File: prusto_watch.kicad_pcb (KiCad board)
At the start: 4 copper layers, 45.7 x 40.6 mm, 79 parts, among them J1 USB_microB_2040002-1, J3 Conn_02x05_Odd_Even, J4 Vibration Motor, J6 Conn_01x05, Q1 RUM002N02T2L, Q2 RUM002N02T2L, Q3 RUM002N02T2L, SW1 SW_Push, SW2 SW_Push, U1 STM32F303RCT6-48, U2 TPS2113ADRBR, U3 TSP70933DBVR, U4 MCP73831T-2ACI, U5 AT42QT1070-MMHR, U6 TPS60241DGKR, U7 RT9818A-18GV, U8 WM1389CT-ND, U9 LSM6DSL, Y1 ECS.327, Y2 FA-238

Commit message: Basic positioning
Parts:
- removed C27: 100nF, Capacitors_SMD:C_0603
- removed J6: Conn_01x05, Pin_Headers:Pin_Header_Straight_1x05_Pitch1.00mm
- removed R17, R18, R19, R20, R21, R22, R23: 10K, Resistors_SMD:R_0603
- removed R24: 4.75K, Resistors_SMD:R_0603
- removed R25: 1K, Resistors_SMD:R_0603
- removed R26: 100K, Resistors_SMD:R_0603
- removed U9: LSM6DSL, Housings_LGA:Bosch_LGA-14_3x2.5mm_Pitch0.5mm
- added J2: Conn_02x05_Odd_Even, Pin_Headers:Pin_Header_Straight_2x05_Pitch1.00mm, F.Cu at (117.8, 51.5)
- added J5: Conn_01x08, Pin_Headers:Pin_Header_Straight_1x08_Pitch2.54mm, F.Cu at (134.6, 163.8)
- BT1: value Battery_Cell -> RJD3032HPPV30M
- C1, C10, C11, C12, C13, C14, C15, C16, C18, C19, C2, C26, C3, C4, C5, C6, C7, C8, C9, R10, R2, R9: moved to F.Cu
- C17, C21: value 100nF -> 1uF; footprint Capacitors_SMD:C_0603 -> Capacitors_SMD:C_0805; moved to F.Cu
- C20, C22, C23: value 1uF -> 100nF; footprint Capacitors_SMD:C_0805 -> Capacitors_SMD:C_0603; moved to F.Cu
- C24: value 10uF -> 1uF; moved to F.Cu
- C25: value 100nF -> 10uF; footprint Capacitors_SMD:C_0603 -> Capacitors_SMD:C_0805; moved to F.Cu
- D2: footprint open_watch:SMLP34RGB2W3 -> prusto_watch:SMLP34RGB2W3
- FP1: footprint open_watch:BM71BLES1FC2 -> prusto_watch:BM71BLES1FC2
- J1: footprint open_watch:USB_microB_2040002-1 -> prusto_watch:USB_microB_2040002-1
- J3: value Conn_02x05_Odd_Even -> Vibration Motor; footprint Pin_Headers:Pin_Header_Straight_2x05_Pitch1.00mm -> Pin_Headers:Pin_Header_Straight_1x02_Pitch1.00mm
- J4: value Vibration Motor -> Conn_01x06; footprint Pin_Headers:Pin_Header_Straight_1x02_Pitch1.00mm -> Pin_Headers:Pin_Header_Straight_1x06_Pitch2.54mm
- Q1, Q2, Q3: footprint open_watch:VMT3 -> prusto_watch:VMT3
- R1: value 10K -> 100K; moved to F.Cu
- R11: value DNP-0 -> 1K; moved to F.Cu
- R12: value 100K -> DNP-0; moved to F.Cu
- R14: value 10K -> 4.75K
- R15: value 10K -> 1K
- R3: value 402 -> 10K; moved to F.Cu
- R4: value 200K -> 100K; moved to F.Cu
- R5: value 470 -> 402; moved to F.Cu
- R6: value 1K -> 200K; moved to F.Cu
- R7: value 1K -> 470; moved to F.Cu
- R8: value 10K -> 1K; moved to F.Cu
- SW1, SW2: footprint open_watch:PTS820_J15M_SMTR_LFS -> prusto_watch:PTS820_J15M_SMTR_LFS
- U2: footprint open_watch:SON-8 -> prusto_watch:SON-8
- U5: value AT42QT1070-MMHR -> TPS60241DGKR; footprint open_watch:AT42QT1070-MMHR -> Housings_SSOP:MSOP-8_3x3mm_Pitch0.65mm
- U6: value TPS60241DGKR -> LSM6DSL; footprint Housings_SSOP:MSOP-8_3x3mm_Pitch0.65mm -> Housings_LGA:Bosch_LGA-14_3x2.5mm_Pitch0.5mm
- U8: footprint open_watch:Molex_FPC_5034801000 -> prusto_watch:Molex_FPC_5034801000
- Y1: footprint open_watch:ECX-31B -> prusto_watch:ECX-31B
- moved R2 178.5 mm to (242.3, 108.0)
- moved R1 176.6 mm to (232.1, 119.5), turned to 0 degrees
- moved C5 169.8 mm to (223.3, 111.3)
- moved D3 169.7 mm to (210.6, 121.3), turned to 0 degrees
- moved R13 169.4 mm to (215.6, 137.3), turned to 0 degrees
- moved R10 164.1 mm to (212.6, 38.1), turned to 0 degrees
- moved Q2 154.1 mm to (203.6, 111.3)
- moved U6 148.2 mm to (186.7, 155.5)
- moved C14 145.6 mm to (213.6, 43.2), turned to 0 degrees
- moved C23 141.0 mm to (193.6, 157.5)
- moved C22 140.7 mm to (189.8, 149.9), turned to 0 degrees
- moved BT1 140.7 mm to (190.6, 112.3), turned to 0 degrees
- moved R7 140.6 mm to (210.1, 48.3), turned to 0 degrees
- moved J3 140.5 mm to (207.0, 105.6), turned to 0 degrees
- moved Q3 140.0 mm to (184.2, 119.4), turned to 0 degrees
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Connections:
- C18 pad 1: +3V3 -> Net-(C18-Pad1)
- C18 pad 2: GND -> Net-(C18-Pad2)
- C20 pad 1: Net-(C20-Pad1) -> +5V
- C20 pad 2: Net-(C20-Pad2) -> GND
- C22 pad 1: +5V -> +3V3
- C23 pad 1: /BLE_nRST -> +3V3
- C24 pad 1: GND -> /BLE_nRST
- C24 pad 2: +3V3 -> GND
- C25 pad 1: /DISP_EN -> GND
- C25 pad 2: GND -> +3V3
- C26 pad 1: +3V3 -> /DISP_EN
- J3 pad 2: /TMS -> Net-(D3-Pad2)
- J4 pad 2: Net-(D3-Pad2) -> /RX_BLE
- R1 pad 1: Net-(R1-Pad1) -> /VUSB
- R10 pad 1: +3V3 -> Net-(R10-Pad1)
- R10 pad 2: /NRST_TOUCH -> GND
- R11 pad 1: +3V3 -> Net-(D2-Pad4)
- R11 pad 2: Net-(C12-Pad1) -> /LED_GREEN
- R12 pad 1: /VUSB -> +3V3
- R12 pad 2: GND -> Net-(C12-Pad1)
- R13 pad 1: /BATT_EN -> /MOTOR_EN
- R14 pad 1: /TOUCH_1 -> +3V3
- R14 pad 2: Net-(R14-Pad2) -> /BLE_nRST
- R15 pad 1: /TOUCH_2 -> +3V3
- R15 pad 2: Net-(R15-Pad2) -> Net-(D4-Pad2)
- R16 pad 1: /TOUCH_3 -> +3V3
- R16 pad 2: Net-(R16-Pad2) -> /STM_NRST
- R2 pad 1: Net-(R2-Pad1) -> /BATT_EN
- R4 pad 1: /VUSB -> Net-(R4-Pad1)
- R4 pad 2: Net-(R2-Pad1) -> GND
- R5 pad 2: Net-(D1-Pad1) -> GND
- R6 pad 1: Net-(D2-Pad2) -> /VUSB
- R6 pad 2: /LED_RED -> Net-(R4-Pad1)
- R7 pad 1: Net-(D2-Pad3) -> Net-(R7-Pad1)
- R7 pad 2: /LED_BLUE -> Net-(D1-Pad1)
- R8 pad 1: Net-(R8-Pad1) -> Net-(D2-Pad2)
- R8 pad 2: GND -> /LED_RED
- R9 pad 1: Net-(D2-Pad4) -> Net-(D2-Pad3)
- R9 pad 2: /LED_GREEN -> /LED_BLUE
- SW1 pad 2: Net-(R1-Pad1) -> Net-(R3-Pad1)
- U1 pad 41: /TOUCH_0 -> Net-(U1-Pad41)
- U1 pad 42: /TOUCH_4 -> Net-(U1-Pad42)
- U1 pad 43: /TOUCH_3 -> Net-(U1-Pad43)
- U1 pad 44: Net-(R1-Pad1) -> Net-(R3-Pad1)
- U1 pad 45: /TOUCH_2 -> Net-(U1-Pad45)
- U1 pad 46: /TOUCH_1 -> Net-(U1-Pad46)
- U2 pad 3: Net-(R2-Pad1) -> Net-(R4-Pad1)
- U2 pad 4: Net-(R3-Pad1) -> Net-(R5-Pad1)
- U4 pad 1: Net-(R5-Pad1) -> Net-(R7-Pad1)
- U4 pad 5: Net-(R8-Pad1) -> Net-(R10-Pad1)
- U5 pad 1: Net-(R23-Pad2) -> +5V
- U5 pad 2: Net-(R22-Pad2) -> /5V_EN
- U5 pad 3: Net-(R21-Pad2) -> Net-(C19-Pad2)
- U5 pad 4: Net-(R20-Pad2) -> GND
- U5 pad 5: Net-(R19-Pad2) -> Net-(C18-Pad2)
- U5 pad 6: Net-(U5-Pad6) -> +3V3
- U5 pad 7: Net-(U5-Pad7) -> Net-(C18-Pad1)
- U5 pad 8: GND -> Net-(C19-Pad1)
- U6 pad 1: +5V -> /IMU_SDO
- U6 pad 2: /5V_EN -> GND
- U6 pad 3: Net-(C20-Pad2) -> GND
- U6 pad 4: GND -> /IMU_INT_1
- U6 pad 5: Net-(C19-Pad2) -> +3V3
- U6 pad 6: +3V3 -> GND
- U6 pad 7: Net-(C19-Pad1) -> GND
- U6 pad 8: Net-(C20-Pad1) -> +3V3
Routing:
- net GND: track 121.9 -> 0.00 mm, vias 32 -> 0
- net +3V3: track 69.5 -> 0.00 mm, vias 16 -> 0
- net /VUSB: track 44.2 -> 0.00 mm, vias 6 -> 0
- net /STM_NRST: track 43.1 -> 0.00 mm, vias 3 -> 0
- net +5V: track 29.1 -> 0.00 mm, vias 2 -> 0
- net /VBATT: track 28.4 -> 0.00 mm, vias 1 -> 0
- net Net-(R1-Pad1): track 25.0 -> 0.00 mm, vias 3 -> 0
- net /BLE_nRST: track 21.7 -> 0.00 mm, vias 3 -> 0
- net /5V_EN: track 20.3 -> 0.00 mm, vias 2 -> 0
- net /DISP_EN: track 18.6 -> 0.00 mm, vias 2 -> 0
- net /EXTCOMIN: track 18.1 -> 0.00 mm, vias 4 -> 0
- net /DISP_SCLK: track 16.4 -> 0.00 mm
- net /D_N: track 16.4 -> 0.00 mm
- net /D_P: track 16.4 -> 0.00 mm
- net /IMU_INT_2: track 16.3 -> 0.00 mm, vias 2 -> 0
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- removed copper zone on In1.Cu, net +3V3
- removed copper zone on In2.Cu, net GND
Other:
- board outline removed
- copper layers 4 -> 2
- net class Default: clearance 0.1016 -> 0.2; trace_width 0.2032 -> 0.25
- rule pad_to_mask_clearance: 0.2 -> 0
- rule trace_clearance: 0.1016 -> 0.2

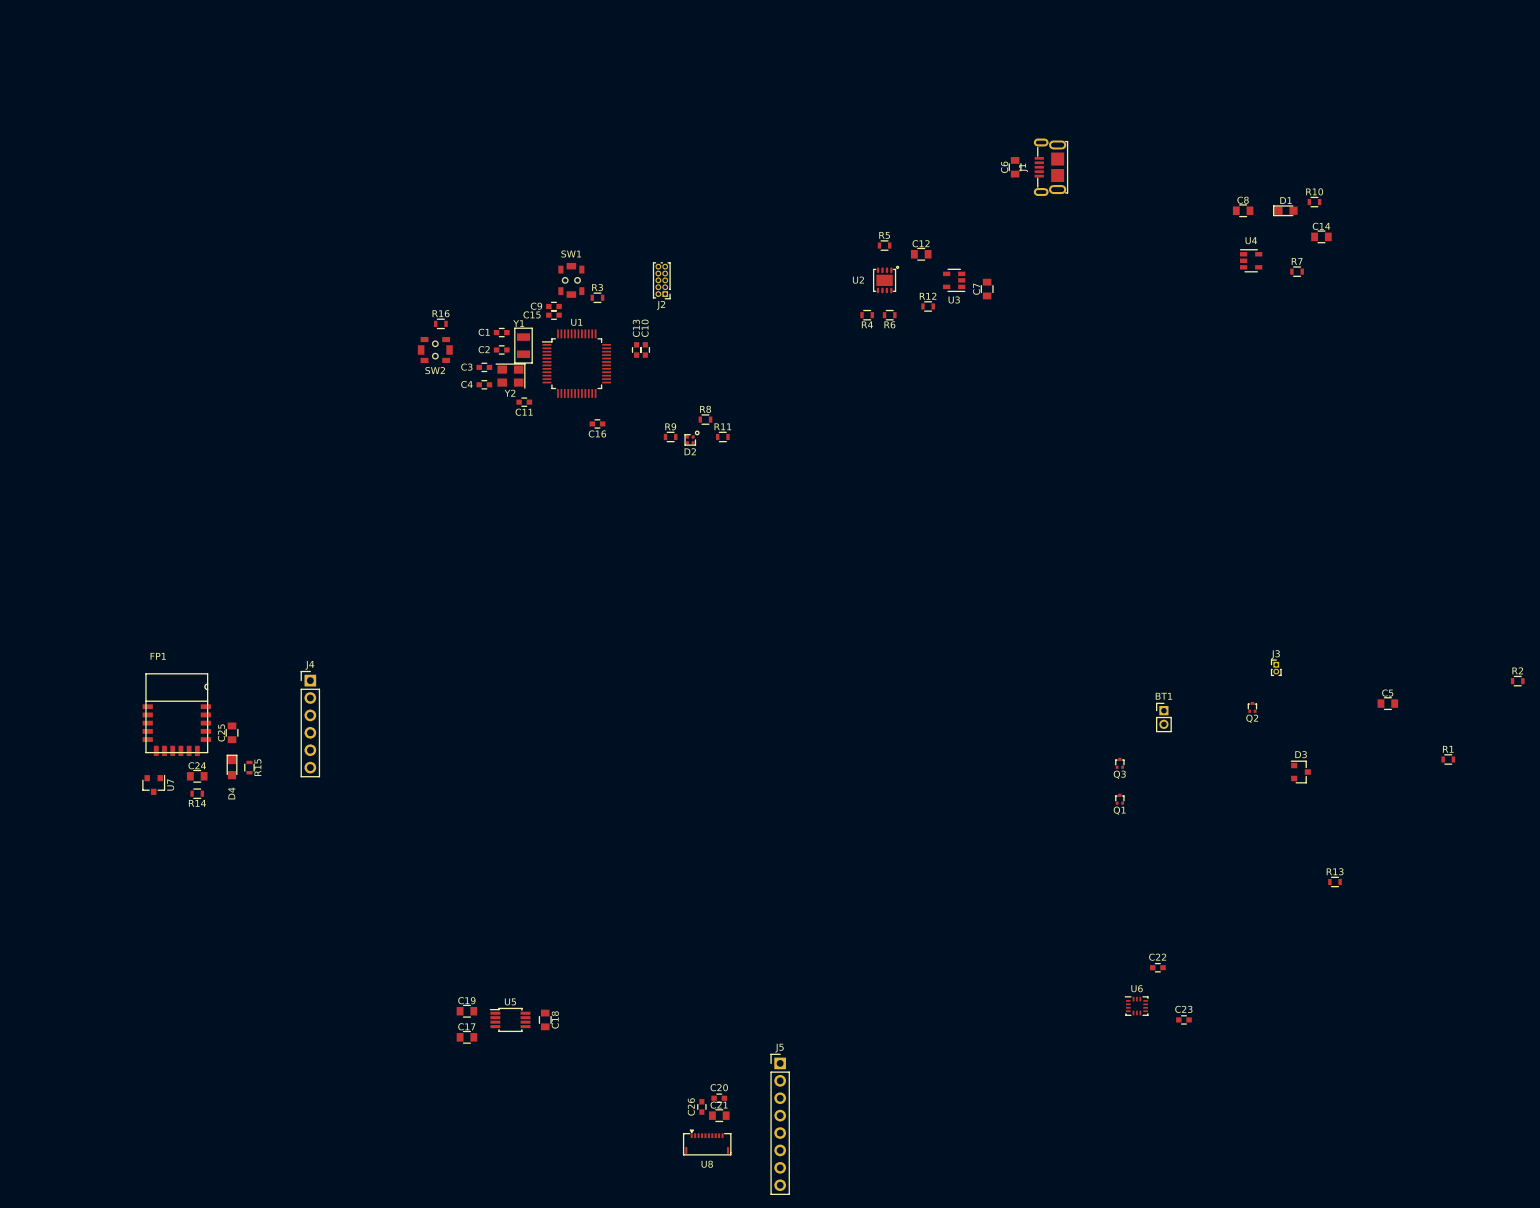
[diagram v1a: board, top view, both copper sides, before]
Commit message: Update footprints
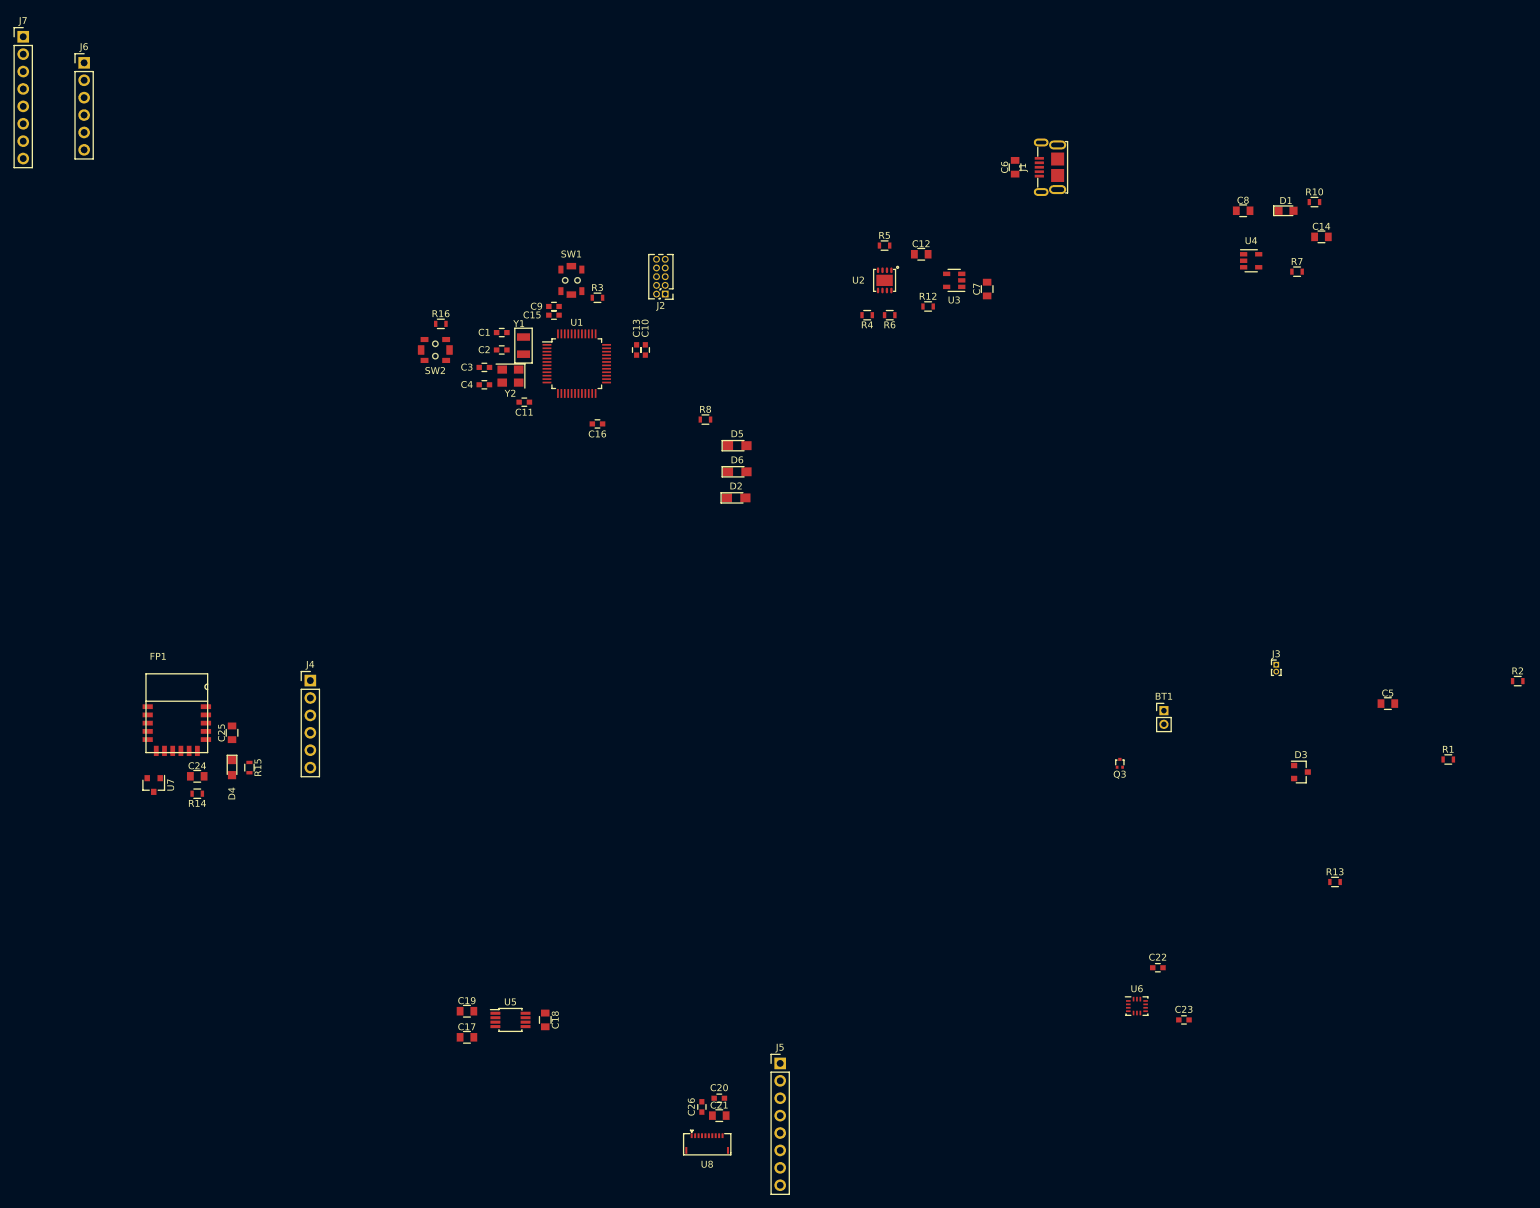
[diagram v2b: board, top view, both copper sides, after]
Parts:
- removed Q1, Q2: RUM002N02T2L, prusto_watch:VMT3
- removed R11, R9: 1K, Resistors_SMD:R_0603
- added D5: LED, LEDs:LED_0805_HandSoldering, F.Cu at (128.3, 73.7)
- added D6: LED, LEDs:LED_0805_HandSoldering, F.Cu at (128.3, 77.5)
- added J6: Conn_01x06, Pin_Headers:Pin_Header_Straight_1x06_Pitch2.54mm, F.Cu at (33.0, 17.8)
- added J7: Conn_01x08, Pin_Headers:Pin_Header_Straight_1x08_Pitch2.54mm, F.Cu at (24.1, 14.0)
- D2: value LED_ARGB -> LED; footprint prusto_watch:SMLP34RGB2W3 -> LEDs:LED_0805_HandSoldering
- J2: footprint Pin_Headers:Pin_Header_Straight_2x05_Pitch1.00mm -> Pin_Headers:Pin_Header_Straight_2x05_Pitch1.27mm
- R1, R2: value 100K -> 1K
- moved D2 10.8 mm to (128.2, 81.3)
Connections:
- BT1 pad 2: Net-(BT1-Pad2) -> GND
- D2 pad 1: +3V3 -> Net-(D2-Pad1)
- D2 pad 2: Net-(D2-Pad2) -> +3V3
- FP1 pad 11: Net-(FP1-Pad11) -> /BLE_P0_0
- FP1 pad 15: Net-(FP1-Pad15) -> /BLE_P2_7
- FP1 pad 3: Net-(FP1-Pad3) -> /BLE_P1_2
- FP1 pad 4: Net-(FP1-Pad4) -> /BLE_P1_3
- FP1 pad 5: Net-(FP1-Pad5) -> /BLE_P1_7
- FP1 pad 6: Net-(FP1-Pad6) -> /BLE_P1_6
- FP1 pad 9: Net-(FP1-Pad9) -> /BLE_P3_6
- R1 pad 1: /VUSB -> Net-(D2-Pad1)
- R1 pad 2: GND -> /LED_1
- R2 pad 1: /BATT_EN -> Net-(D5-Pad1)
- R2 pad 2: GND -> /LED_2
- R8 pad 1: Net-(D2-Pad2) -> Net-(D6-Pad1)
- R8 pad 2: /LED_RED -> /LED_3
- U1 pad 12: Net-(U1-Pad12) -> /DISP_SCS
- U1 pad 16: /IMU_SDO -> Net-(U1-Pad16)
- U1 pad 2: Net-(U1-Pad2) -> /DISP_EN
- U1 pad 20: /DISP_SCS -> Net-(U1-Pad20)
- U1 pad 25: /BLE_nRST -> Net-(U1-Pad25)
- U1 pad 26: /BLE_CONF -> /IMU_SCL
- U1 pad 27: /DISP_EN -> /IMU_SDO
- U1 pad 28: /EXTCOMIN -> /IMU_SDI
- U1 pad 29: /LED_RED -> /LED_1
- U1 pad 30: /LED_GREEN -> /LED_2
- U1 pad 31: /LED_BLUE -> /LED_3
- U1 pad 40: /BATT_EN -> /TSC_G5_IO2
- U1 pad 41: Net-(U1-Pad41) -> /BLE_nRST
- U1 pad 42: Net-(U1-Pad42) -> /TSC_G5_IO3
- U1 pad 43: Net-(U1-Pad43) -> /TSC_G5_IO4
- U1 pad 45: Net-(U1-Pad45) -> /BLE_CONF
- U1 pad 46: Net-(U1-Pad46) -> /EXTCOMIN
- U6 pad 13: /DISP_SCLK -> /IMU_SCL
- U6 pad 14: /DISP_SDI -> /IMU_SDI

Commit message: Finish basic placement
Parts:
- BT1: footprint Pin_Headers:Pin_Header_Straight_1x02_Pitch2.00mm -> prusto_watch:Molex-0532610271
- moved R1 188.4 mm to (62.2, 38.1)
- moved R2 185.1 mm to (69.8, 40.6)
- moved R13 167.3 mm to (67.3, 60.0), turned to 90 degrees
- moved D3 159.7 mm to (62.2, 62.2), turned to 90 degrees
- moved J3 147.7 mm to (63.8, 69.8), turned to 90 degrees
- moved C5 139.4 mm to (110.5, 29.5), turned to 270 degrees
- moved Q3 131.5 mm to (63.6, 66.9), turned to 90 degrees
- moved BT1 119.1 mm to (108.0, 26.7), turned to 180 degrees
- moved J7 94.0 mm to (82.5, 87.6), turned to 270 degrees
- moved R7 85.9 mm to (125.7, 31.8)
- moved R10 85.2 mm to (128.8, 22.9)
- moved C14 85.2 mm to (129.8, 27.9)
- moved C8 85.2 mm to (118.4, 24.1)
- moved D1 85.2 mm to (124.6, 24.1)
- moved U4 84.5 mm to (120.7, 29.2)
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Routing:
- net /D_N: track 0.00 -> 36.1 mm
- net /D_P: track 0.00 -> 36.1 mm

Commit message: Finish routing traces
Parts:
- removed J7: Conn_01x08, Pin_Headers:Pin_Header_Straight_1x08_Pitch2.54mm
- added J8: Conn_01x02, Pin_Headers:Pin_Header_Straight_1x02_Pitch2.54mm, F.Cu at (137.7, 51.8)
- added J9: Conn_01x04, Pin_Headers:Pin_Header_Straight_1x04_Pitch2.54mm, F.Cu at (130.6, 62.5)
- J3: footprint Pin_Headers:Pin_Header_Straight_1x02_Pitch1.00mm -> Pin_Headers:Pin_Header_Straight_1x02_Pitch2.54mm
- moved J4 74.4 mm to (129.5, 74.2)
- moved FP1 65.6 mm to (134.4, 79.9), turned to 270 degrees
- moved C25 57.6 mm to (138.7, 93.5), turned to 90 degrees
- moved C24 45.1 mm to (130.8, 89.9), turned to 270 degrees
- moved U7 43.2 mm to (127.0, 88.9)
- moved D4 43.2 mm to (129.4, 94.0), turned to 180 degrees
- moved R15 38.1 mm to (124.5, 94.0)
- moved R14 36.1 mm to (122.4, 86.6)
- moved C21 32.4 mm to (91.5, 91.4), turned to 180 degrees
- moved C23 31.4 mm to (125.7, 69.1)
- moved C20 30.1 mm to (91.7, 94.5), turned to 180 degrees
- moved U6 29.7 mm to (120.4, 68.1)
- moved U8 28.7 mm to (98.8, 95.5)
- moved C19 27.9 mm to (81.8, 88.9), turned to 90 degrees
- moved U5 27.5 mm to (85.3, 88.9)
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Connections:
- FP1 pad 11: /BLE_P0_0 -> Net-(FP1-Pad11)
- FP1 pad 15: /BLE_P2_7 -> Net-(FP1-Pad15)
- FP1 pad 3: /BLE_P1_2 -> Net-(FP1-Pad3)
- FP1 pad 4: /BLE_P1_3 -> Net-(FP1-Pad4)
- FP1 pad 5: /BLE_P1_7 -> Net-(FP1-Pad5)
- FP1 pad 6: /BLE_P1_6 -> Net-(FP1-Pad6)
- FP1 pad 9: /BLE_P3_6 -> Net-(FP1-Pad9)
- U1 pad 13: /IMU_CS -> /DISP_EN
- U1 pad 18: /IMU_INT_1 -> /LED_3
- U1 pad 19: /IMU_INT_2 -> /BLE_CONF
- U1 pad 2: /DISP_EN -> /LED_1
- U1 pad 20: Net-(U1-Pad20) -> /BLE_nRST
- U1 pad 29: /LED_1 -> /IMU_CS
- U1 pad 30: /LED_2 -> /IMU_INT_1
- U1 pad 31: /LED_3 -> /IMU_INT_2
- U1 pad 41: /BLE_nRST -> Net-(U1-Pad41)
- U1 pad 45: /BLE_CONF -> /LED_2
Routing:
- net +3V3: track 0.00 -> 339.8 mm, vias 0 -> 8
- net GND: track 0.00 -> 97.9 mm, vias 0 -> 52
- net /5V_EN: track 0.00 -> 86.6 mm
- net /BLE_CONF: track 0.00 -> 75.0 mm, vias 0 -> 8
- net /VUSB: track 0.00 -> 68.5 mm, vias 0 -> 2
- net /BLE_nRST: track 0.00 -> 67.7 mm, vias 0 -> 4
- net /STM_NRST: track 0.00 -> 58.8 mm, vias 0 -> 2
- net /TX_BLE: track 0.00 -> 50.9 mm, vias 0 -> 2
- net /EXTCOMIN: track 0.00 -> 49.5 mm, vias 0 -> 6
- net /RX_BLE: track 0.00 -> 47.9 mm, vias 0 -> 2
- net /DISP_EN: track 0.00 -> 45.4 mm, vias 0 -> 2
- net /DISP_SCS: track 0.00 -> 43.4 mm
- net /DISP_SDI: track 0.00 -> 43.2 mm
- net /DISP_SCLK: track 0.00 -> 42.8 mm, vias 0 -> 2
- net +5V: track 0.00 -> 42.1 mm
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- added copper zone on B.Cu, net GND
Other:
- board outline added: 78.7 x 74.9 mm
- net class Default: trace_width 0.25 -> 0.254
- board text added: ""GND""
- board text added: "3.3V"
- board text added: "5V"
- board text added: "5V_EN"
- board text added: "BLE_CONF"
- board text added: "BLE_nRST"
- board text added: "DISP_EN"
- board text added: "DISP_SCLK"
- board text added: "DISP_SCS"
- board text added: "DISP_SDI"
- board text added: "EXTCOMIN"
- board text added: "GND"
- board text added: "IMU_CS"
- board text added: "IMU_SCL"
- board text added: "IMU_SDI"
- board text added: "Prog"
- board text added: "PrustoWatch v0.2 BW"
- board text added: "RX_BLE"
- board text added: "SDO"
- board text added: "TSC_G5_IO2"
- board text added: "TSC_G5_IO3"
- board text added: "TSC_G5_IO4"
- board text added: "TX_BLE"
- board text added: "USB_N"
- board text added: "USB_P"
